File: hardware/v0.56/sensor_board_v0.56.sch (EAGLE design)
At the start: 63 parts, among them J3 USB-MICROB, U10 TSL2591, U11 915MHz, U3 OPA344, U4 SI7021, U5 ATMEGA328P-MU, U6 ADMP401, U7 PMS7003, U8 MCP1703CB, U9 BMP280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

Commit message: update
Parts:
- added R9: 100K, Adafruit Feather 32u4 Bluefruit LE:MICROBUILDER_RESISTOR_0402MP
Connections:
- new net A1: U5.PC1
- new net A2: U5.PC2
- new net A3: U5.PC3
- new net A6: U5.ADC6
- new net A7: U5.ADC7
- new net N$13: R9.2, U$7.ADDR
- net D5: now also U$7.WAKE
- net GND: now also C2.1, J2.1, U$7.GND
- net PWR: now also J2.2
- net SCL: now also U$7.SCL
- net SDA: now also U$7.SDA
- net VCC: now also C2.2, R9.1, U$7.VDD
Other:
- note added: "3.3V Power"
- note added: "5V Power"
- note removed: "Power"
- note removed: "headers"
- moved on the sheet: R13, R6

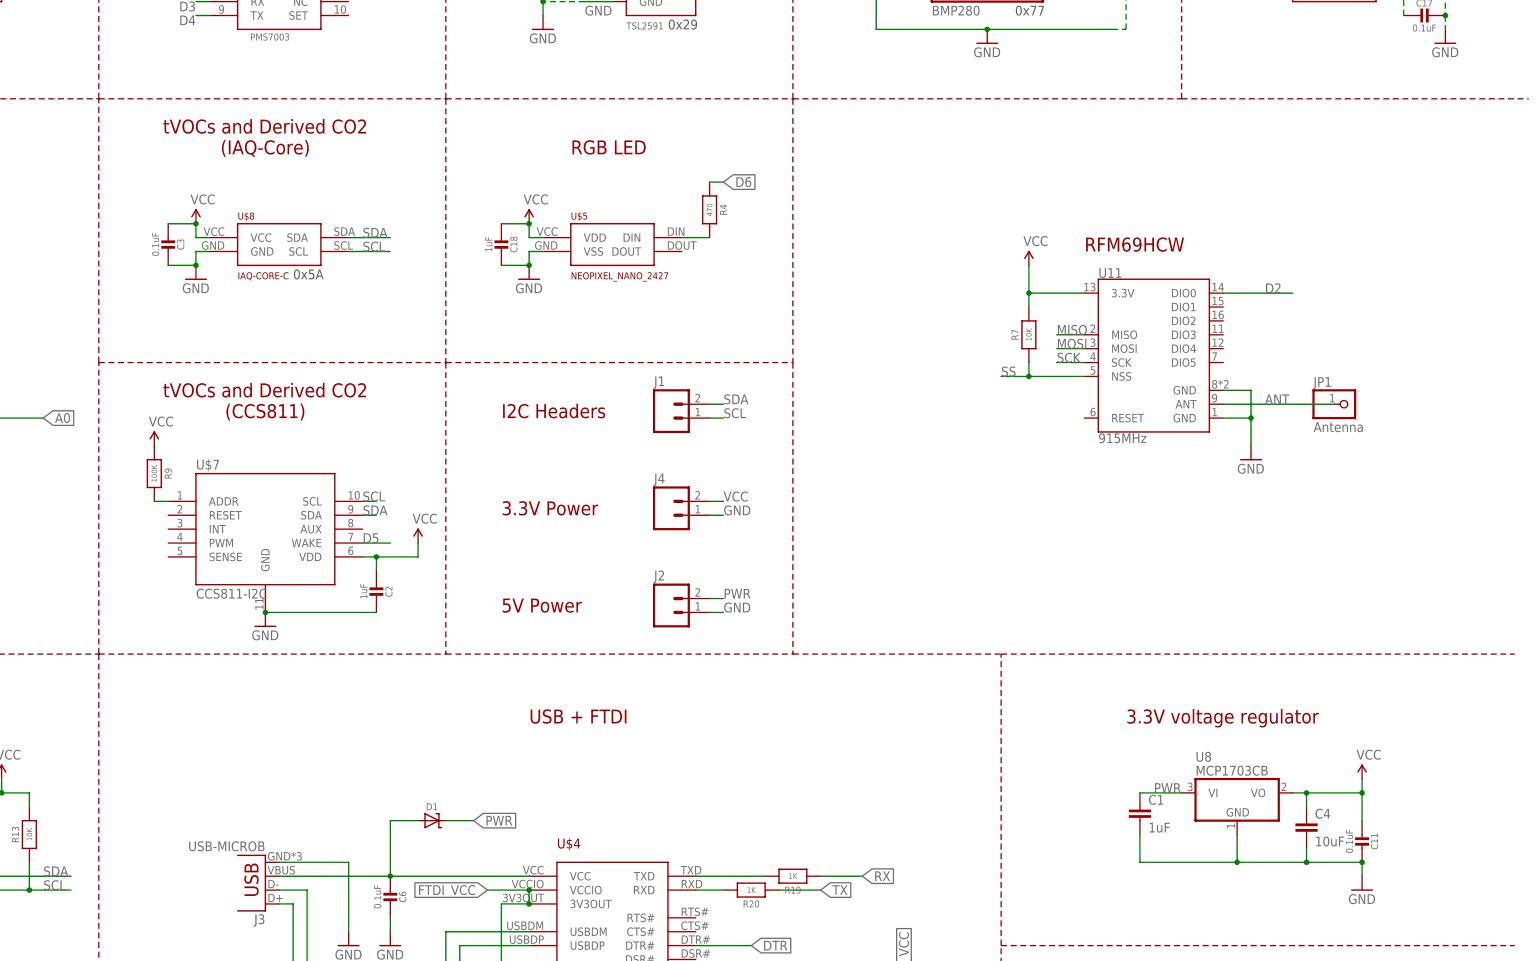
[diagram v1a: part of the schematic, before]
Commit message: Added Power Booster circuit; a lot of rearrangments
circuit traces still incomplete
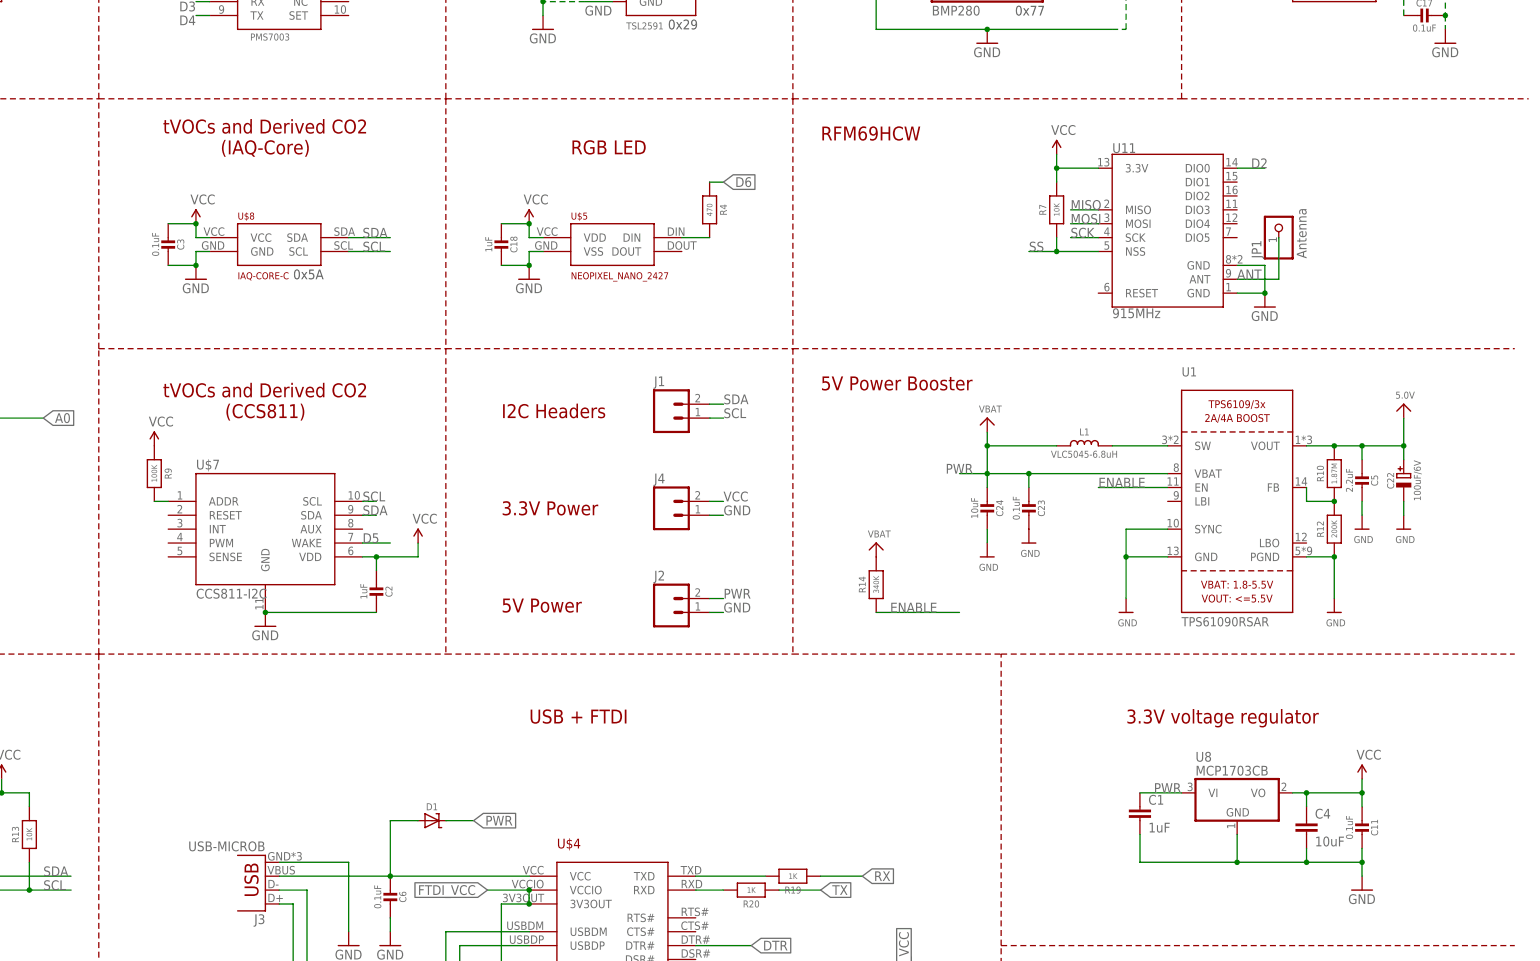
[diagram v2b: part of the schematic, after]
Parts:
- added C22: 100uF/6V, microbuilder:CAP_TANTALUMB/3528_REFLOW
- added C23: 0.1uF, Adafruit Feather 32u4 Bluefruit LE:MICROBUILDER_CAP_CERAMIC_0402MP
- added C24: 10uF, Adafruit Feather 32u4 Bluefruit LE:MICROBUILDER_CAP_CERAMIC_0402MP
- added C5: 2.2uF, Adafruit Feather 32u4 Bluefruit LE:MICROBUILDER_CAP_CERAMIC_0402MP
- added L1: VLC5045-6.8uH, microbuilder:INDUCTORTDK_VLC5045
- added R10: 1.87M, Adafruit Feather 32u4 Bluefruit LE:MICROBUILDER_RESISTOR_0402MP
- added R12: 200K, Adafruit Feather 32u4 Bluefruit LE:MICROBUILDER_RESISTOR_0402MP
- added R14: 340K, Adafruit Feather 32u4 Bluefruit LE:MICROBUILDER_RESISTOR_0402MP
- added U1: TPS61090RSAR, microbuilder:VREG_TPS6103X
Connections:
- new net 5.0V: C22.+, C5.2, R10.2, U1.VOUT
- new net ENABLE: R14.1, U1.EN
- new net N$12: R10.1, R12.2, U1.FB
- new net N$6: L1.2, U1.SW
- new net VBAT: R14.2
- net GND: now also C22.-, C23.1, C24.1, C5.1, R12.1, U1.GND, U1.PGND, U1.SYNC
- net PWR: now also C23.2, C24.2, L1.1, U1.VBAT
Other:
- note added: "5V Power Booster"
- moved on the sheet: C11, JP1, R7, U11

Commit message: Adjustments
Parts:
- removed J4: (no value), SparkFun-Connectors:M02PTH
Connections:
- removed net 5.0V: C22.+, C5.2, R10.2, U1.VOUT
- new net 5V: C17.2, C22.+, C5.2, R10.2, U$6.VIN, U1.VOUT
- net GND: now also U1.LBI; no longer J4.1
- net PWR: no longer C17.2, U$6.VIN
- net VCC: no longer J4.2
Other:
- note removed: "3.3V Power"

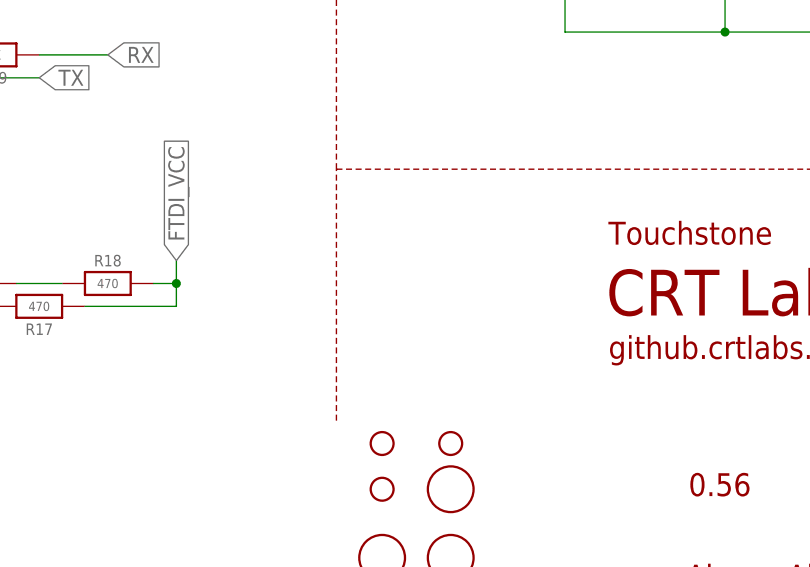
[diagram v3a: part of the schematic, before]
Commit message: Added notches in the board
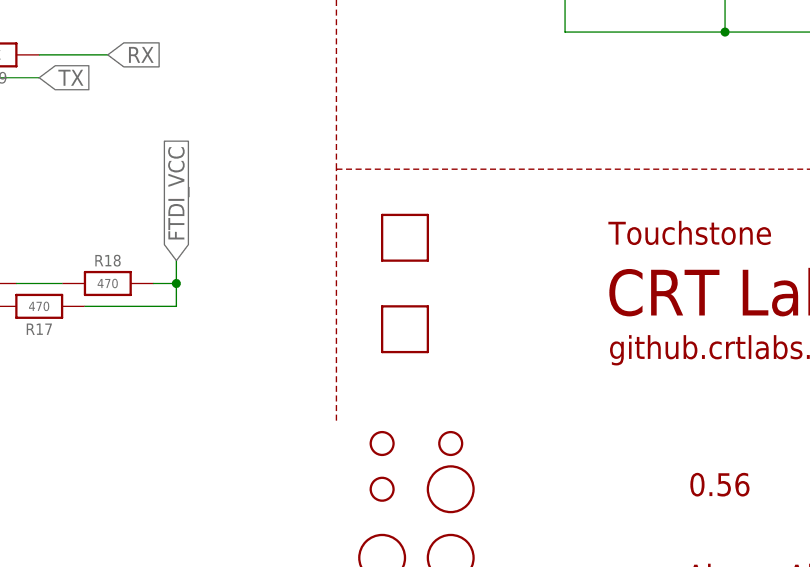
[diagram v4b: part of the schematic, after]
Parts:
- added U$12, U$9: VLP-450-F, VLP-450-F:VLP-450-F
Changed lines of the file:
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@@
 <grid distance="0.1" unitdist="inch" unit="inch" style="lines" multiple="1" display="no" altdistance="0.01" altunitdist="inch" altunit="inch"/>
 <layers>
-<layer number="1" name="Top" color="4" fill="1" visible="yes" active="no"/>
-<layer number="2" name="Route2" color="1" fill="3" visible="yes" active="no"/>
-<layer number="3" name="Route3" color="4" fill="3" visible="yes" active="no"/>
-<layer number="4" name="Route4" color="1" fill="4" visible="yes" active="no"/>
-<layer number="5" name="Route5" color="4" fill="4" visible="yes" active="no"/>
-<layer number="6" name="Route6" color="1" fill="8" visible="yes" active="no"/>
-<layer number="7" name="Route7" color="4" fill="8" visible="yes" active="no"/>
-<layer number="8" name="Route8" color="1" fill="2" visible="yes" active="no"/>
-<layer number="9" name="Route9" color="4" fill="2" visible="yes" active="no"/>
-<layer number="10" name="Route10" color="1" fill="7" visible="yes" active="no"/>
-<layer number="11" name="Route11" color="4" fill="7" visible="yes" active="no"/>
-<layer number="12" name="Route12" color="1" fill="5" visible="yes" active="no"/>
-<layer number="13" name="Route13" color="4" fill="5" visible="yes" active="no"/>
-<layer number="14" name="Route14" color="1" fill="6" visible="yes" active="no"/>
-<layer number="15" name="Route15" color="4" fill="6" visible="yes" active="no"/>
-<layer number="16" name="Bottom" color="1" fill="1" visible="yes" active="no"/>
-<layer number="17" name="Pads" color="2" fill="1" visible="yes" active="no"/>
-<layer number="18" name="Vias" color="2" fill="1" visible="yes" active="no"/>
-<layer number="19" name="Unrouted" color="6" fill="1" visible="yes" active="no"/>
-<layer number="20" name="Dimension" color="15" fill="1" visible="yes" active="no"/>
-<layer number="21" name="tPlace" color="7" fill="1" visible="yes" active="no"/>
-<layer number="22" name="bPlace" color="7" fill="1" visible="yes" active="no"/>
-<layer number="23" name="tOrigins" color="15" fill="1" visible="yes" active="no"/>
-<layer number="24" name="bOrigins" color="15" fill="1" visible="yes" active="no"/>
-<layer number="25" name="tNames" color="7" fill="1" visible="yes" active="no"/>
-<layer number="26" name="bNames" color="7" fill="1" visible="yes" active="no"/>
-<layer number="27" name="tValues" color="7" fill="1" visible="yes" active="no"/>
-<layer number="28" name="bValues" color="7" fill="1" visible="yes" active="no"/>
+<layer number="1" name="Top" color="4" fill="1" visible="no" active="no"/>
+<layer number="2" name="Route2" color="1" fill="3" visible="no" active="no"/>
+<layer number="3" name="Route3" color="4" fill="3" visible="no" active="no"/>
+<layer number="4" name="Route4" color="1" fill="4" visible="no" active="no"/>
+<layer number="5" name="Route5" color="4" fill="4" visible="no" active="no"/>
+<layer number="6" name="Route6" color="1" fill="8" visible="no" active="no"/>
+<layer number="7" name="Route7" color="4" fill="8" visible="no" active="no"/>
+<layer number="8" name="Route8" color="1" fill="2" visible="no" active="no"/>
+<layer number="9" name="Route9" color="4" fill="2" visible="no" active="no"/>
+<layer number="10" name="Route10" color="1" fill="7" visible="no" active="no"/>
+<layer number="11" name="Route11" color="4" fill="7" visible="no" active="no"/>
+<layer number="12" name="Route12" color="1" fill="5" visible="no" active="no"/>
+<layer number="13" name="Route13" color="4" fill="5" visible="no" active="no"/>
+<layer number="14" name="Route14" color="1" fill="6" visible="no" active="no"/>
+<layer number="15" name="Route15" color="4" fill="6" visible="no" active="no"/>
+<layer number="16" name="Bottom" color="1" fill="1" visible="no" active="no"/>
+<layer number="17" name="Pads" color="2" fill="1" visible="no" active="no"/>
+<layer number="18" name="Vias" color="2" fill="1" visible="no" active="no"/>
+<layer number="19" name="Unrouted" color="6" fill="1" visible="no" active="no"/>
+<layer number="20" name="Dimension" color="15" fill="1" visible="no" active="no"/>
+<layer number="21" name="tPlace" color="7" fill="1" visible="no" active="no"/>
+<layer number="22" name="bPlace" color="7" fill="1" visible="no" active="no"/>
+<layer number="23" name="tOrigins" color="15" fill="1" visible="no" active="no"/>
+<layer number="24" name="bOrigins" color="15" fill="1" visible="no" active="no"/>
+<layer number="25" name="tNames" color="7" fill="1" visible="no" active="no"/>
+<layer number="26" name="bNames" color="7" fill="1" visible="no" active="no"/>
+<layer number="27" name="tValues" color="7" fill="1" visible="no" active="no"/>
+<layer number="28" name="bValues" color="7" fill="1" visible="no" active="no"/>
 <layer number="29" name="tStop" color="7" fill="3" visible="no" active="no"/>
 <layer number="30" name="bStop" color="7" fill="6" visible="no" active="no"/>
@@
 <layer number="35" name="tGlue" color="7" fill="4" visible="no" active="no"/>
 <layer number="36" name="bGlue" color="7" fill="5" visible="no" active="no"/>
-<layer number="37" name="tTest" color="7" fill="1" visible="yes" active="no"/>
-<layer number="38" name="bTest" color="7" fill="1" visible="yes" active="no"/>
+<layer number="37" name="tTest" color="7" fill="1" visible="no" active="no"/>
+<layer number="38" name="bTest" color="7" fill="1" visible="no" active="no"/>
 <layer number="39" name="tKeepout" color="4" fill="11" visible="no" active="no"/>
 <layer number="40" name="bKeepout" color="1" fill="11" visible="no" active="no"/>
@@
 <layer number="44" name="Drills" color="7" fill="1" visible="no" active="no"/>
 <layer number="45" name="Holes" color="7" fill="1" visible="no" active="no"/>
-<layer number="46" name="Milling" color="3" fill="1" visible="yes" active="no"/>
-<layer number="47" name="Measures" color="7" fill="1" visible="yes" active="no"/>
-<layer number="48" name="Document" color="7" fill="1" visible="yes" active="no"/>
-<layer number="49" name="Reference" color="7" fill="1" visible="yes" active="no"/>
-<layer number="50" name="dxf" color="7" fill="1" visible="yes" active="no"/>
-<layer number="51" name="tDocu" color="7" fill="1" visible="yes" active="no"/>
-<layer number="52" name="bDocu" color="7" fill="1" visible="yes" active="no"/>
-<layer number="53" name="tGND_GNDA" color="7" fill="9" visible="yes" active="no"/>
-<layer number="54" name="bGND_GNDA" color="1" fill="9" visible="yes" active="no"/>
-<layer number="56" name="wert" color="7" fill="1" visible="yes" active="no"/>
-<layer number="57" name="tCAD" color="7" fill="1" visible="yes" active="no"/>
-<layer number="59" name="tCarbon" color="7" fill="1" visible="yes" active="no"/>
-<layer number="60" name="bCarbon" color="7" fill="1" visible="yes" active="no"/>
+<layer number="46" name="Milling" color="3" fill="1" visible="no" active="no"/>
+<layer number="47" name="Measures" color="7" fill="1" visible="no" active="no"/>
+<layer number="48" name="Document" color="7" fill="1" visible="no" active="no"/>
+<layer number="49" name="Reference" color="7" fill="1" visible="no" active="no"/>
+<layer number="50" name="dxf" color="7" fill="1" visible="no" active="no"/>
+<layer number="51" name="tDocu" color="7" fill="1" visible="no" active="no"/>
+<layer number="52" name="bDocu" color="7" fill="1" visible="no" active="no"/>
+<layer number="53" name="tGND_GNDA" color="7" fill="9" visible="no" active="no"/>
+<layer number="54" name="bGND_GNDA" color="1" fill="9" visible="no" active="no"/>
+<layer number="56" name="wert" color="7" fill="1" visible="no" active="no"/>
+<layer number="57" name="tCAD" color="7" fill="1" visible="no" active="no"/>
+<layer number="59" name="tCarbon" color="7" fill="1" visible="no" active="no"/>
+<layer number="60" name="bCarbon" color="7" fill="1" visible="no" active="no"/>
 <layer number="90" name="Modules" color="5" fill="1" visible="yes" active="yes"/>
 <layer number="91" name="Nets" color="2" fill="1" visible="yes" active="yes"/>
@@
 <part name="R12" library="Adafruit Feather 32u4 Bluefruit LE" deviceset="MICROBUILDER_RESISTOR" device="_0402MP" value="200K"/>
 <part name="R14" library="Adafruit Feather 32u4 Bluefruit LE" deviceset="MICROBUILDER_RESISTOR" device="_0402MP" value="340K"/>
+<part name="U$9" library="VLP-450-F" deviceset="VLP-450-F" device=""/>
+<part name="U$12" library="VLP-450-F" deviceset="VLP-450-F" device=""/>
 </parts>
 <sheets>
@@
 <instance part="R12" gate="G$1" x="279.4" y="10.16" rot="R90"/>
 <instance part="R14" gate="G$1" x="195.58" y="0" rot="R90"/>
+<instance part="U$9" gate="G$1" x="226.06" y="-73.66"/>
+<instance part="U$12" gate="G$1" x="226.06" y="-83.82"/>
 </instances>
 <busses>
